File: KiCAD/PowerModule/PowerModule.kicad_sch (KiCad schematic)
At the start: 41 parts, among them J1 GPU, J2 BATTERY, J3 BUS, J4 MONITOR, J5 MASTER, J6 Conn_01x02, J7 Conn_01x02, Q3 AO3401A, Q5 AO3401A, U2 INA219BxDCN, U3 INA219BxDCN, U4 INA219BxDCN

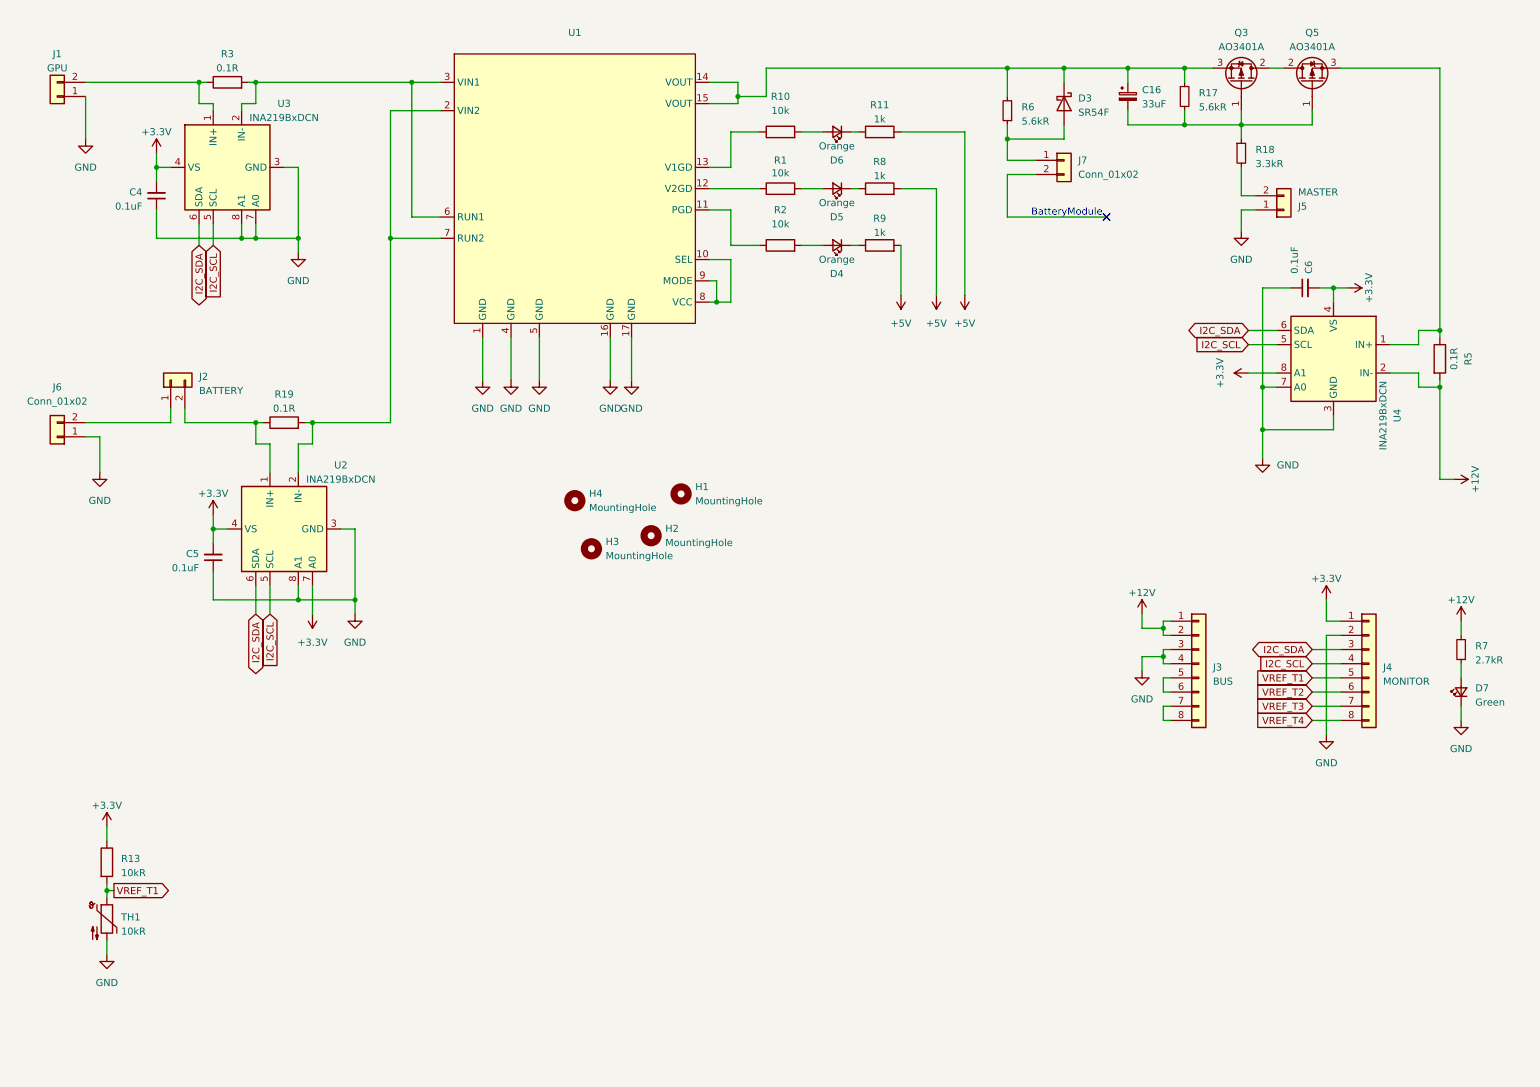
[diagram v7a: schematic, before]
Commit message: 取り付け穴位置を更新
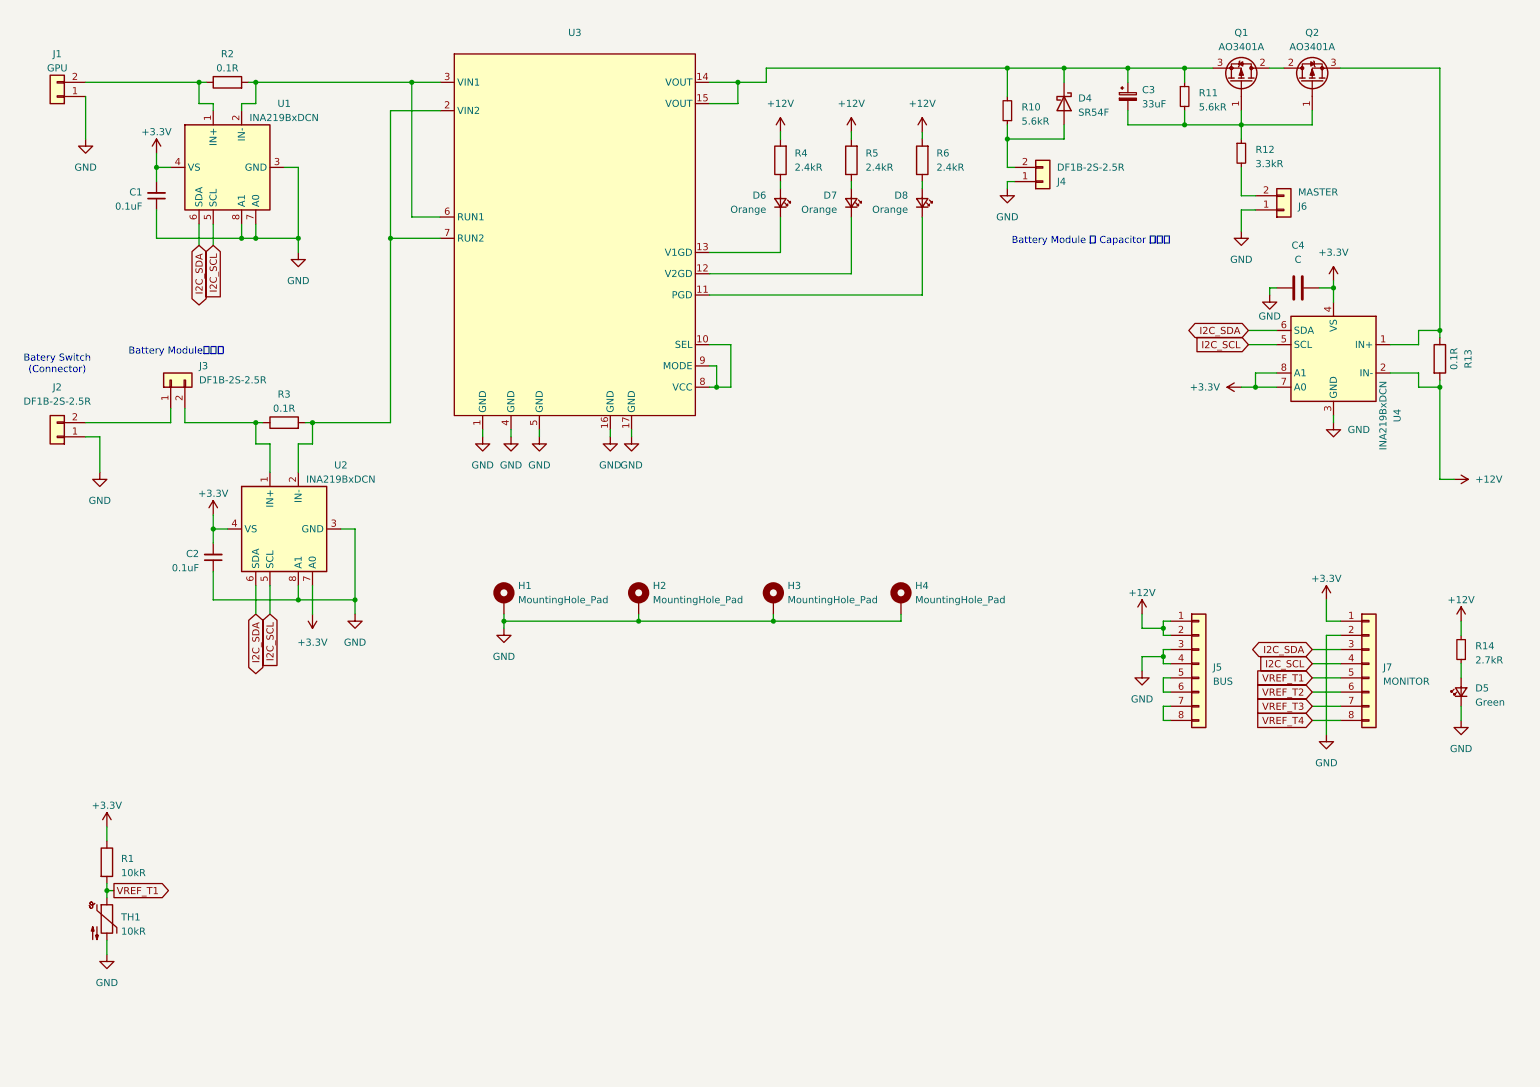
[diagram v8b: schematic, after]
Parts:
- removed C6: 0.1uF, Capacitor_SMD:C_0603_1608Metric_Pad1.08x0.95mm_HandSolder, symbol Device:C_Small
- removed D4, D5: Orange, LED_SMD:LED_0603_1608Metric_Pad1.05x0.95mm_HandSolder, symbol Device:LED_Small
- removed H1, H2, H3, H4: MountingHole, MountingHole:MountingHole_3.2mm_M3_DIN965_Pad_TopBottom, symbol Mechanical:MountingHole
- removed R1, R2: 10k, Resistor_SMD:R_0603_1608Metric, symbol Device:R
- removed R11, R8, R9: 1k, Resistor_SMD:R_0603_1608Metric, symbol Device:R
- added C4: C, symbol Device:C
- added D7, D8: Orange, LED_SMD:LED_0603_1608Metric, symbol Device:LED_Small
- added H1, H2, H3, H4: MountingHole_Pad, MountingHole:MountingHole_3.2mm_M3_DIN965_Pad_TopBottom, symbol Mechanical:MountingHole_Pad
- added R5, R6: 2.4kR, Resistor_SMD:R_0603_1608Metric, symbol Device:R
- D6: footprint LED_SMD:LED_0603_1608Metric_Pad1.05x0.95mm_HandSolder -> LED_SMD:LED_0603_1608Metric
- J2: renamed from J6; value Conn_01x02 -> DF1B-2S-2.5R
- J3: renamed from J2; value BATTERY -> DF1B-2S-2.5R
- J4: renamed from J7; value Conn_01x02 -> DF1B-2S-2.5R
- R4: renamed from R10; value 10k -> 2.4kR
- renumbered C4 to C1, C5 to C2, C16 to C3, D3 to D4, D7 to D5, J3 to J5, J5 to J6, J4 to J7, Q3 to Q1, Q5 to Q2, R13 to R1, R6 to R10, R17 to R11, R18 to R12, R5 to R13, R7 to R14, R3 to R2, R19 to R3, U3 to U1, U1 to U3
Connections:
- net +12V: now also R4.2, R5.2, R6.2
- net +3.3V: now also U4.7 (A0), C4.2
- net GND: now also J4.1 (Pin_1), C4.1, H1.1, H2.1, H3.1, H4.1; no longer U4.7 (A0)
- net at D6.1 (K): now also U3.13 (V1GD)
- net at D6.2 (A): now also R4.1; no longer R4.2
- net at D4.2 (A), R10.1: now also J4.2 (Pin_2); no longer J4.1 (Pin_1)
- net at U3.12 (V2GD): now also D7.1 (K)
- net at U3.11 (PGD): now also D8.1 (K)
- new net: D7.2 (A), R5.1
- new net: D8.2 (A), R6.1
- no-connect marks 1 -> 0
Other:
- note added: "Batery Switch (Connector)"
- note added: "Battery Module の Capacitor に接続"
- note added: "Battery Moduleに接続"
- note removed: "BatteryModule"
- moved on the sheet: J4, R4, U3
